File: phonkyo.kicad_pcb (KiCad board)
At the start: 2 copper layers, 65 x 30 mm, 31 parts, among them J1 GPIO, J2 LineOutJack, J4 RIJack, U2 PCM5102A, U3 XC6206P332MR

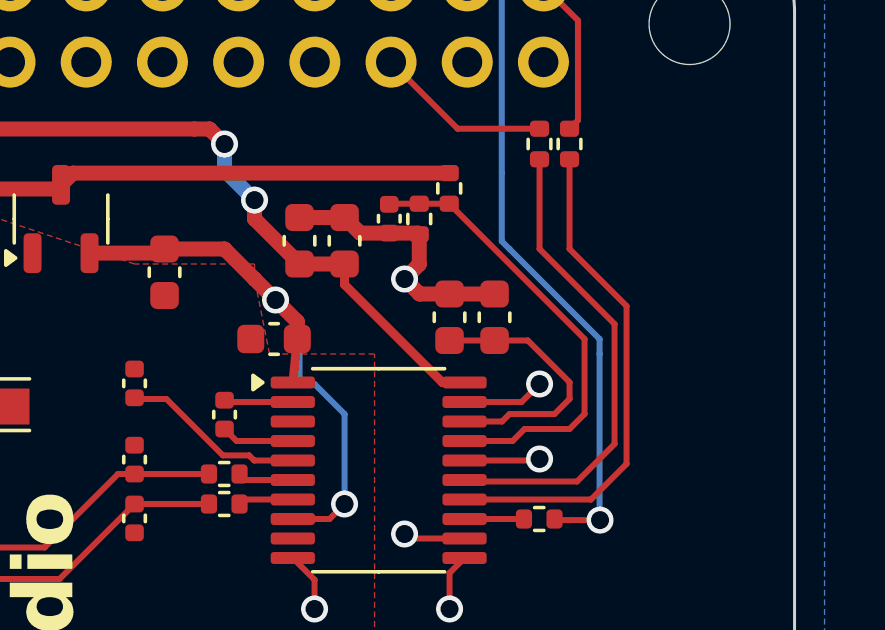
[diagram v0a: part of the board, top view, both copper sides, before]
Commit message: pcb: put C11 on DVDD pin 20 and shorten the LDOO route
C11, the 100 nF decoupling cap on DVDD (pin 20), sat 6.0 mm of track
from its pin. That track was a diagonal from (150, 80.7), because the
area above the right column was taken by C12/C13 (the LDOO caps) and
the LDOO route looped around pins 19 and 20 to reach pin 18.

Re-laid out the right-hand fan-out:

- C11 sits directly above pin 20. Track to the pin: 6.0 mm -> 1.1 mm.
- C12 and C13 move beside C11. LDOO runs straight down beside the pins
  to pin 18, replacing the loop. C12 to pin 18: 9.0 mm -> 3.9 mm.
- Pin 19 (DGND) previously ran right to a via in the middle of that
  area. It now goes under the chip body to a via between the pad rows,
  where the board already has two vias.
- The three cap grounds share a new stitching via just above them.

C11 and C12 change from 0603 to 0402. Values are unchanged (100 nF),
and 0402 has lower inductance, which is the point of decoupling. The
schematic footprint fields are updated to match. C13 (10 uF bulk) stays
0603. The new 0402 footprints are cloned from C4 so they match the
board's existing 0402 parts.

XSMT, LRCK and DIN are untouched.

Semantic diff: 3 footprints changed (C11, C12, C13), none added or
removed, 16 tracks/vias replaced by 12, touching only +3V3, GND and
LDOO. DRC with schematic parity matches the baseline: 0 unconnected,
0 parity errors, no new violations.
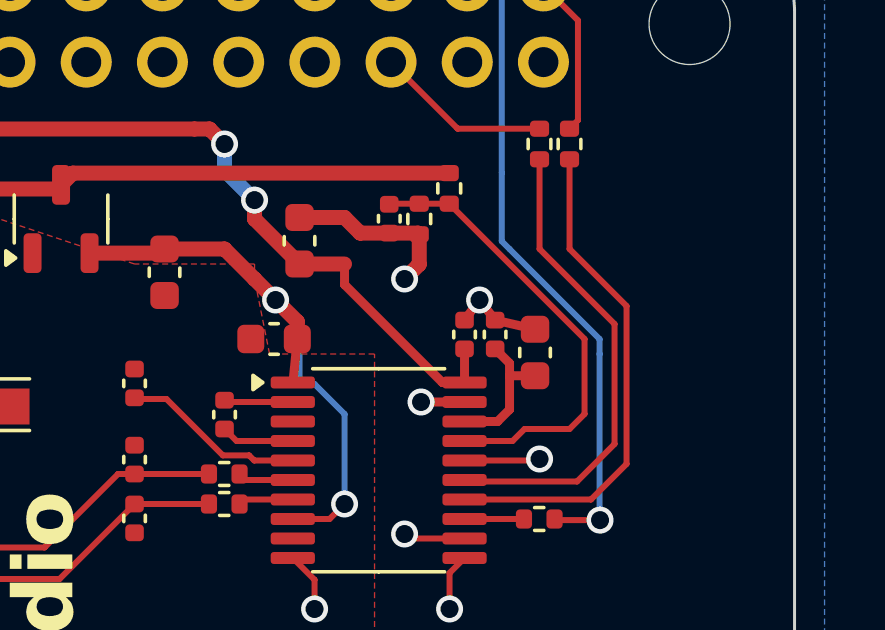
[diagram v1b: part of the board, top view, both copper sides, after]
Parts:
- C11, C12: footprint Capacitor_SMD:C_0603_1608Metric -> Capacitor_SMD:C_0402_1005Metric
- moved C11 5.08 mm to (154.0, 83.8)
- moved C13 1.79 mm to (156.3, 84.5)
- moved C12 1.63 mm to (155.0, 83.8)
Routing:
- net Net-(U2-LDOO): track 8.95 -> 4.73 mm
- net GND: track 31.9 -> 29.8 mm, vias 9 -> 10
- net +3V3: track 53.2 -> 54.3 mm
